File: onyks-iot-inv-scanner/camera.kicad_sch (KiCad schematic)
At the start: 8 parts, among them IC4 SN74AVC16T245DGVR, IC6 SN74AVC16T245DGVR, J1 Conn_01x24_MountingPin, Q3 BC547, U6 TCA9406DC

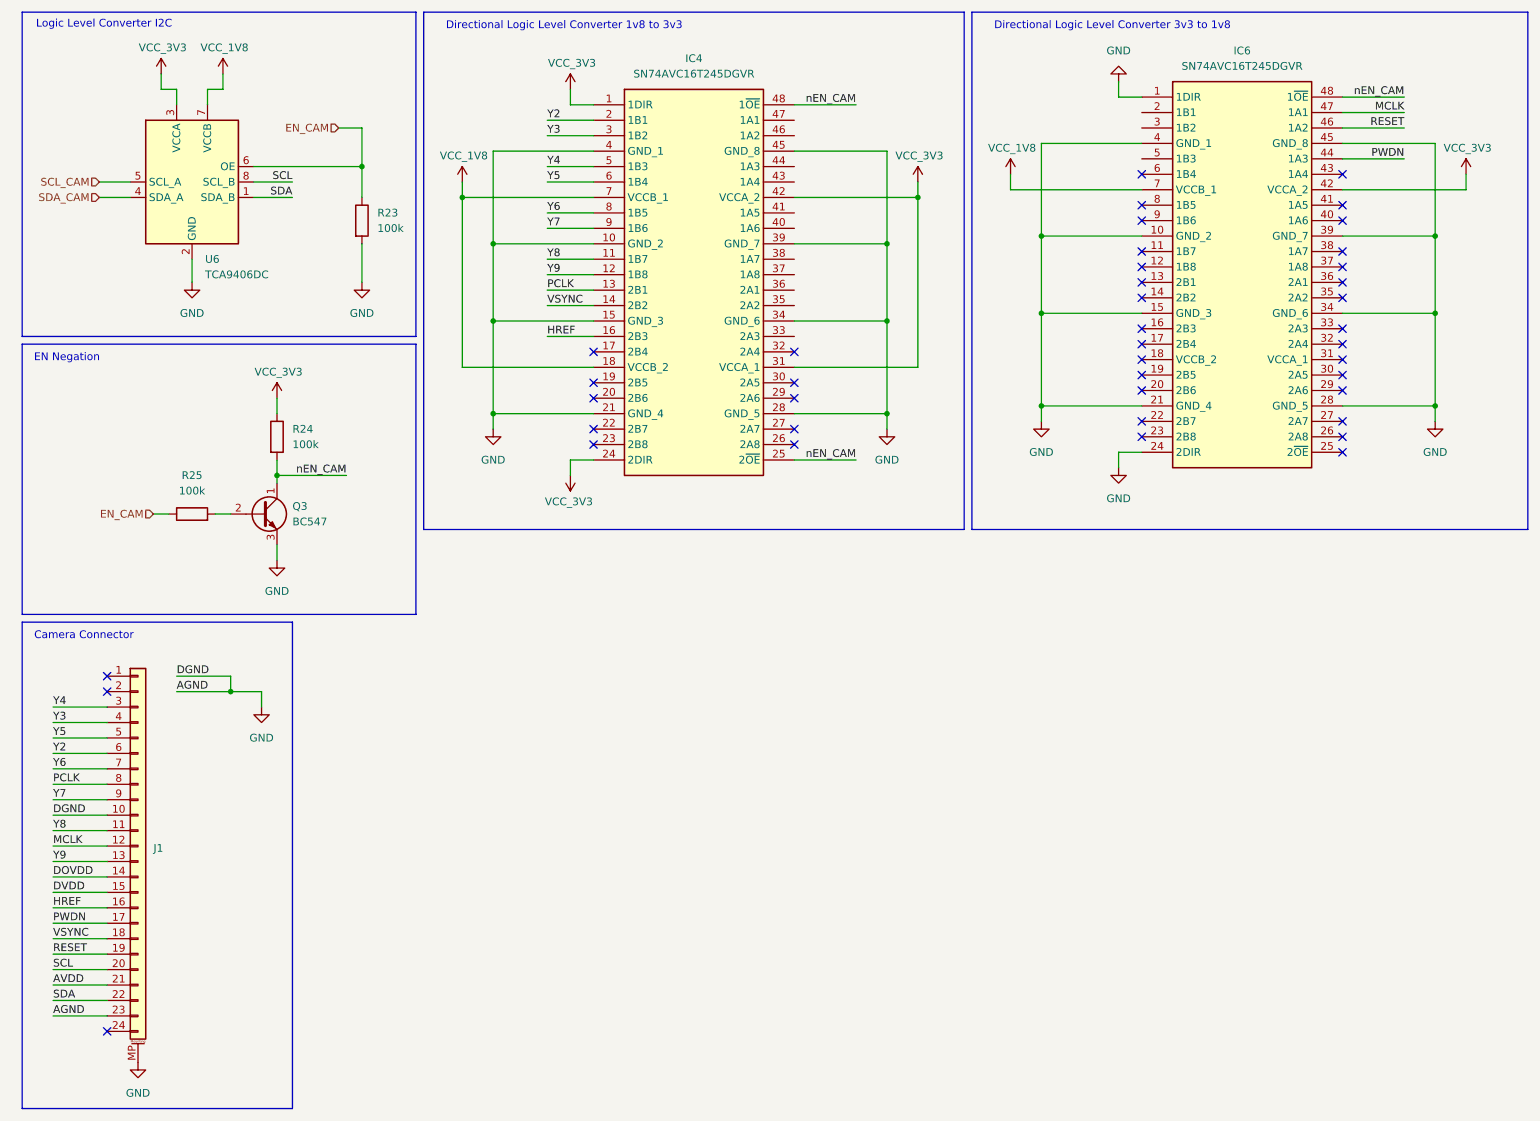
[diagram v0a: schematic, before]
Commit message: added trigger button and connected cammera with llc and power supply
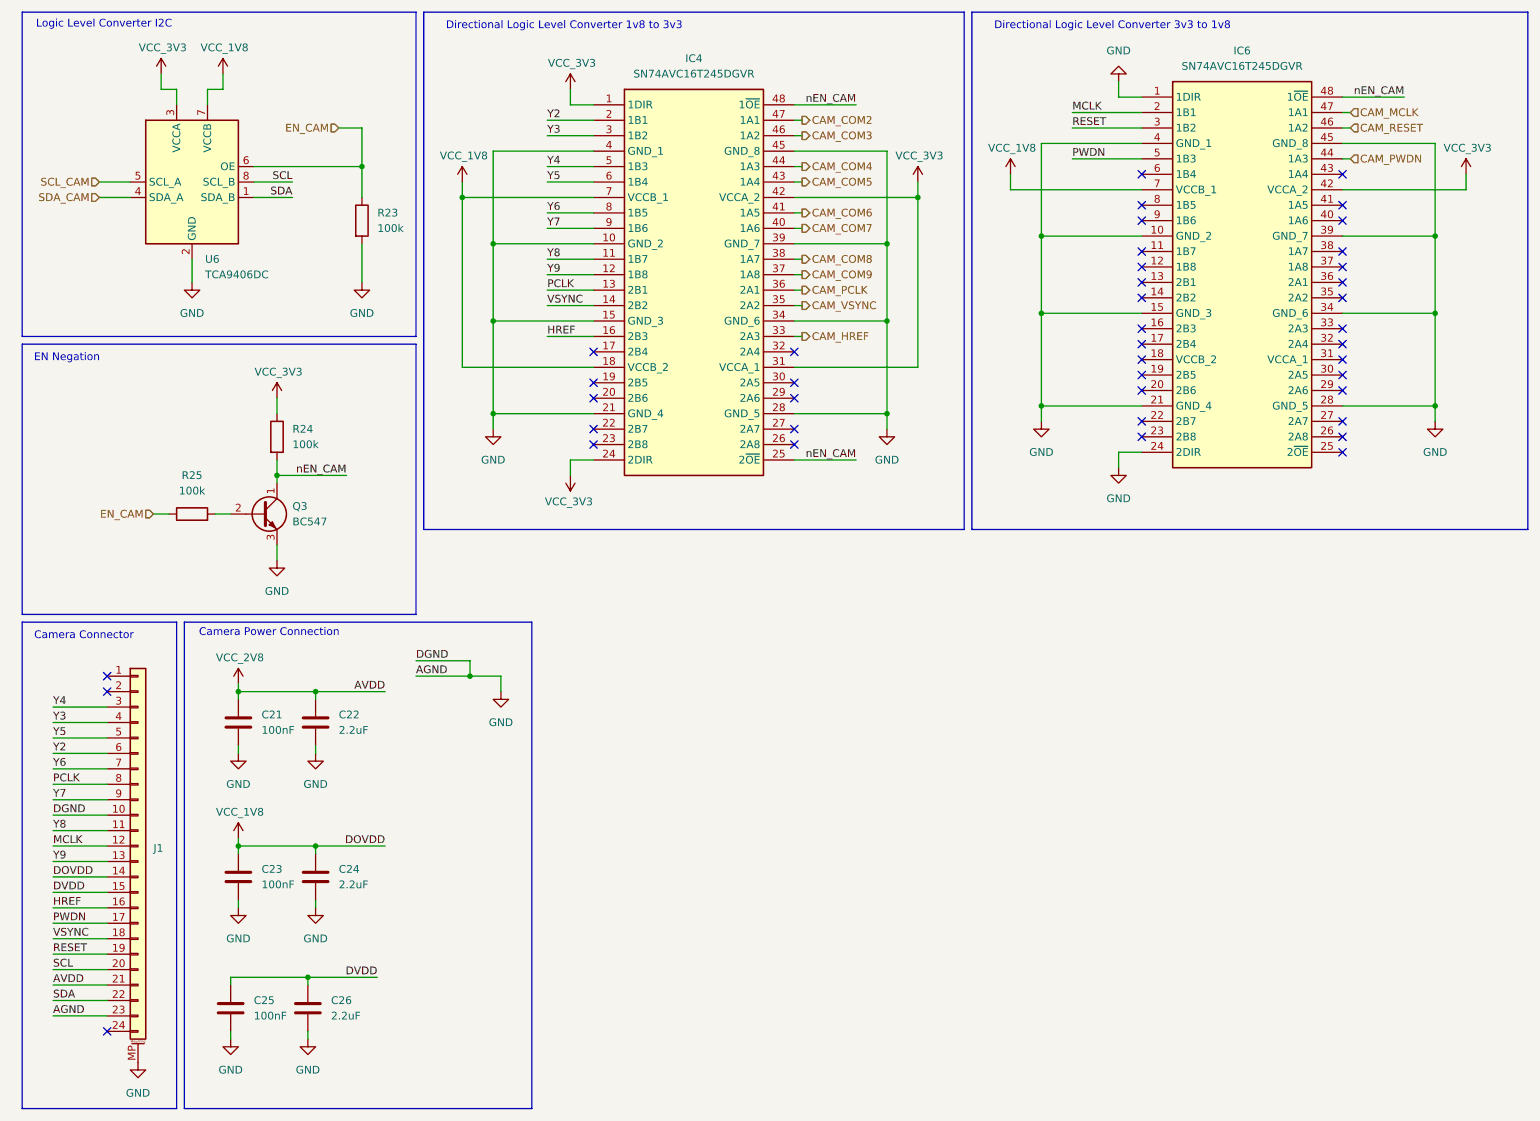
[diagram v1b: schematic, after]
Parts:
- added C21, C23, C25: 100nF, symbol Device:C
- added C22, C24, C26: 2.2uF, symbol Device:C
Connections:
- net DOVDD is gone; now on net VCC_1V8: J1.14 (Pin_14)
- net DVDD: now also C25.1, C26.1
- net GND: now also C21.2, C22.2, C23.2, C24.2, C25.2, C26.2
- net MCLK: now also IC6.2 (1B1); no longer IC6.47 (1A1)
- net PWDN: now also IC6.5 (1B3); no longer IC6.44 (1A3)
- net RESET: now also IC6.3 (1B2); no longer IC6.46 (1A2)
- net VCC_1V8: now also C23.1, C24.1
- net CAM_HREF: now reaches IC4.33 (2A3)
- net CAM_VSYNC: now reaches IC4.35 (2A2)
- net CAM_PCLK: now reaches IC4.36 (2A1)
- net CAM_COM9: now reaches IC4.37 (1A8)
- net CAM_COM8: now reaches IC4.38 (1A7)
- net CAM_COM7: now reaches IC4.40 (1A6)
- net CAM_COM6: now reaches IC4.41 (1A5)
- net CAM_COM5: now reaches IC4.43 (1A4)
- net CAM_COM4: now reaches IC4.44 (1A3)
- net CAM_COM3: now reaches IC4.46 (1A2)
- net CAM_COM2: now reaches IC4.47 (1A1)
- net AVDD renamed VCC_2V8
- net VCC_2V8: now also C21.1, C22.1
- new net CAM_MCLK: IC6.47 (1A1)
- new net CAM_PWDN: IC6.44 (1A3)
- new net CAM_RESET: IC6.46 (1A2)
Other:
- note added: "Camera Power Connection"
